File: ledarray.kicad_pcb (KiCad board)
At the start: 2 copper layers, 37.6 x 52.3 mm, 37 parts, among them J1 Conn_01x14_Male, J2 Conn_01x14_Male

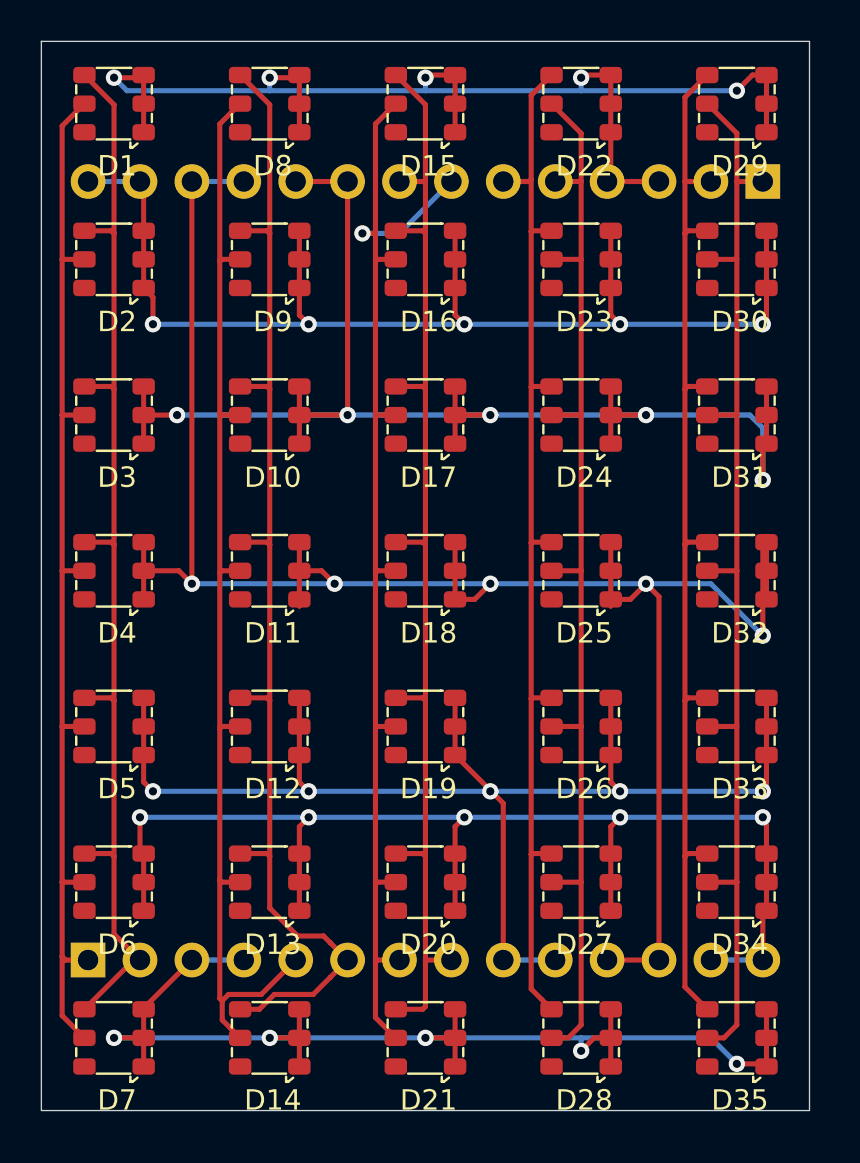
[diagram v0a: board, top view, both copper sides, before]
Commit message: Add reversed LED polarity variant
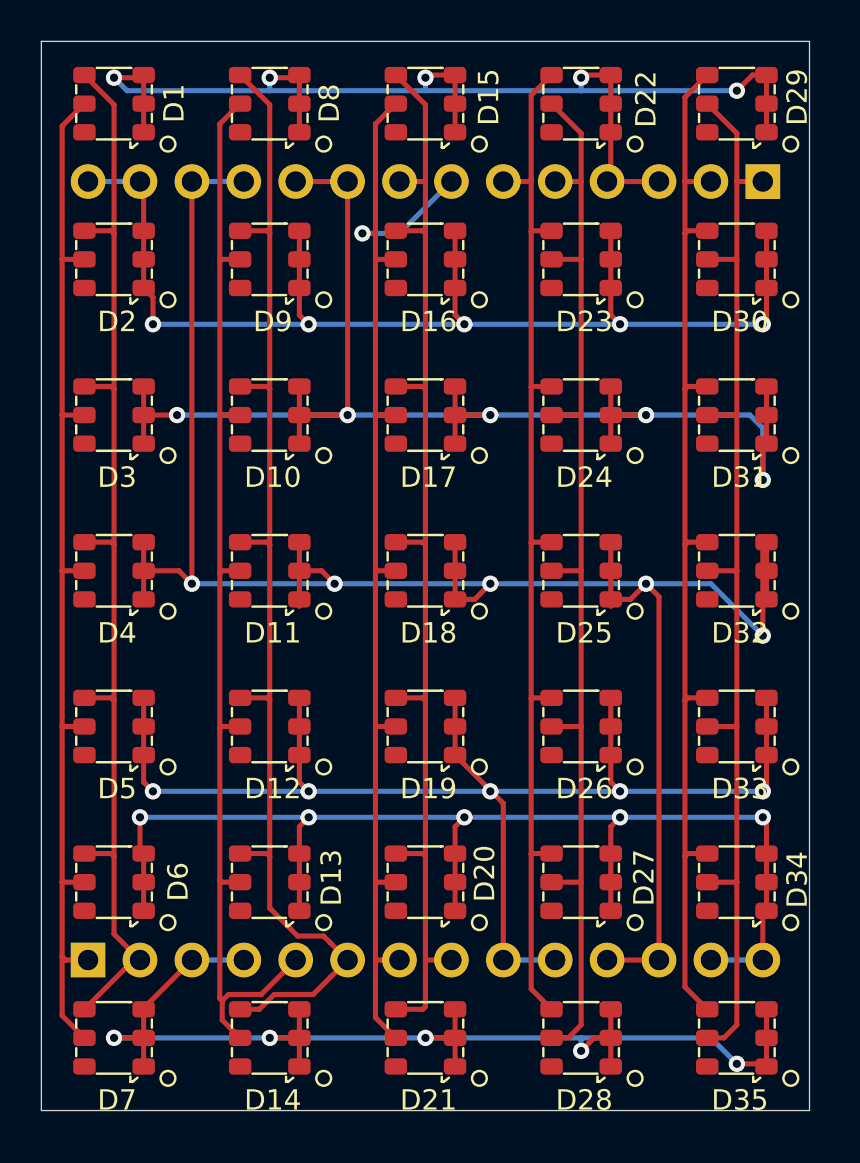
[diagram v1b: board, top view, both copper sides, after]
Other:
- board text added: "Design by Kliment github.com/kliment/5x7RGmatrix COMMON CATHODE VERSION"
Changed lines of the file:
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@@
   (general
     (thickness 1.6)
-    (drawings 4)
+    (drawings 40)
     (tracks 387)
     (zones 0)
@@
     (descr "Through hole straight pin header, 1x14, 2.54mm pitch, single row")
     (tags "Through hole pin header THT 1x14 2.54mm single row")
-    (fp_text reference J2 (at 0 2.33 90) (layer B.SilkS)
+    (fp_text reference J2 (at -2.67 -17.21 180) (layer B.SilkS)
       (effects (font (size 1 1) (thickness 0.15)) (justify mirror))
     )
@@
     (descr "Through hole straight pin header, 1x14, 2.54mm pitch, single row")
     (tags "Through hole pin header THT 1x14 2.54mm single row")
-    (fp_text reference J1 (at 0 2.33 90) (layer B.SilkS)
+    (fp_text reference J1 (at -2.53 -17.01 180) (layer B.SilkS)
       (effects (font (size 1 1) (thickness 0.15)) (justify mirror))
     )
@@
   (module corelib:FM-Z3535RGBA-SH (layer F.Cu)
     (at 180.34 109.22)
-    (fp_text reference D34 (at 0.15 3.05) (layer F.SilkS)
+    (fp_text reference D34 (at 2.96 -0.12 90) (layer F.SilkS)
       (effects (font (size 1 1) (thickness 0.15)))
     )
@@
   (module corelib:FM-Z3535RGBA-SH (layer F.Cu)
     (at 180.34 71.12)
-    (fp_text reference D29 (at 0.15 3.05) (layer F.SilkS)
+    (fp_text reference D29 (at 2.96 -0.32 90) (layer F.SilkS)
       (effects (font (size 1 1) (thickness 0.15)))
     )
@@
   (module corelib:FM-Z3535RGBA-SH (layer F.Cu)
     (at 172.72 109.22)
-    (fp_text reference D27 (at 0.15 3.05) (layer F.SilkS)
+    (fp_text reference D27 (at 3.08 -0.22 90) (layer F.SilkS)
       (effects (font (size 1 1) (thickness 0.15)))
     )
@@
   (module corelib:FM-Z3535RGBA-SH (layer F.Cu)
     (at 172.72 71.12)
-    (fp_text reference D22 (at 0.15 3.05) (layer F.SilkS)
+    (fp_text reference D22 (at 3.18 -0.22 90) (layer F.SilkS)
       (effects (font (size 1 1) (thickness 0.15)))
     )
@@
   (module corelib:FM-Z3535RGBA-SH (layer F.Cu)
     (at 165.1 109.22)
-    (fp_text reference D20 (at 0.15 3.05) (layer F.SilkS)
+    (fp_text reference D20 (at 2.9 -0.42 90) (layer F.SilkS)
       (effects (font (size 1 1) (thickness 0.15)))
     )
@@
   (module corelib:FM-Z3535RGBA-SH (layer F.Cu)
     (at 165.1 71.12)
-    (fp_text reference D15 (at 0.15 3.05) (layer F.SilkS)
+    (fp_text reference D15 (at 3.1 -0.32 90) (layer F.SilkS)
       (effects (font (size 1 1) (thickness 0.15)))
     )
@@
   (module corelib:FM-Z3535RGBA-SH (layer F.Cu)
     (at 157.48 109.22)
-    (fp_text reference D13 (at 0.15 3.05) (layer F.SilkS)
+    (fp_text reference D13 (at 3.02 -0.22 90) (layer F.SilkS)
       (effects (font (size 1 1) (thickness 0.15)))
     )
@@
   (module corelib:FM-Z3535RGBA-SH (layer F.Cu)
     (at 157.48 71.12)
-    (fp_text reference D8 (at 0.15 3.05) (layer F.SilkS)
+    (fp_text reference D8 (at 2.92 -0.02 90) (layer F.SilkS)
       (effects (font (size 1 1) (thickness 0.15)))
     )
@@
   (module corelib:FM-Z3535RGBA-SH (layer F.Cu)
     (at 149.86 109.22)
-    (fp_text reference D6 (at 0.15 3.05) (layer F.SilkS)
+    (fp_text reference D6 (at 3.14 -0.02 90) (layer F.SilkS)
       (effects (font (size 1 1) (thickness 0.15)))
     )
@@
   (module corelib:FM-Z3535RGBA-SH (layer F.Cu)
     (at 149.86 71.12)
-    (fp_text reference D1 (at 0.15 3.05) (layer F.SilkS)
+    (fp_text reference D1 (at 2.94 -0.02 90) (layer F.SilkS)
       (effects (font (size 1 1) (thickness 0.15)))
     )
@@
       (net 4 /17))
   )
+  (gr_text "Design by Kliment\ngithub.com/kliment/5x7RGmatrix\nCOMMON CATHODE VERSION" (at 164.5 93.1) (layer B.SilkS)
+    (effects (font (size 1 1) (thickness 0.15)) (justify mirror))
+  )
+  (gr_circle (center 182.98 118.82) (end 183.18 119.12) (layer F.SilkS) (width 0.12))
+  (gr_circle (center 175.36 118.82) (end 175.56 119.12) (layer F.SilkS) (width 0.12))
+  (gr_circle (center 167.74 118.82) (end 167.94 119.12) (layer F.SilkS) (width 0.12))
+  (gr_circle (center 160.12 118.82) (end 160.32 119.12) (layer F.SilkS) (width 0.12))
+  (gr_circle (center 152.5 118.82) (end 152.7 119.12) (layer F.SilkS) (width 0.12))
+  (gr_circle (center 182.98 111.2) (end 183.18 111.5) (layer F.SilkS) (width 0.12))
+  (gr_circle (center 175.36 111.2) (end 175.56 111.5) (layer F.SilkS) (width 0.12))
+  (gr_circle (center 167.74 111.2) (end 167.94 111.5) (layer F.SilkS) (width 0.12))
+  (gr_circle (center 160.12 111.2) (end 160.32 111.5) (layer F.SilkS) (width 0.12))
+  (gr_circle (center 152.5 111.2) (end 152.7 111.5) (layer F.SilkS) (width 0.12))
+  (gr_circle (center 182.98 103.58) (end 183.18 103.88) (layer F.SilkS) (width 0.12))
+  (gr_circle (center 175.36 103.58) (end 175.56 103.88) (layer F.SilkS) (width 0.12))
+  (gr_circle (center 167.74 103.58) (end 167.94 103.88) (layer F.SilkS) (width 0.12))
+  (gr_circle (center 160.12 103.58) (end 160.32 103.88) (layer F.SilkS) (width 0.12))
+  (gr_circle (center 152.5 103.58) (end 152.7 103.88) (layer F.SilkS) (width 0.12))
+  (gr_circle (center 182.98 95.96) (end 183.18 96.26) (layer F.SilkS) (width 0.12))
+  (gr_circle (center 175.36 95.96) (end 175.56 96.26) (layer F.SilkS) (width 0.12))
+  (gr_circle (center 167.74 95.96) (end 167.94 96.26) (layer F.SilkS) (width 0.12))
+  (gr_circle (center 160.12 95.96) (end 160.32 96.26) (layer F.SilkS) (width 0.12))
+  (gr_circle (center 152.5 95.96) (end 152.7 96.26) (layer F.SilkS) (width 0.12))
+  (gr_circle (center 182.98 88.34) (end 183.18 88.64) (layer F.SilkS) (width 0.12))
+  (gr_circle (center 175.36 88.34) (end 175.56 88.64) (layer F.SilkS) (width 0.12))
+  (gr_circle (center 167.74 88.34) (end 167.94 88.64) (layer F.SilkS) (width 0.12))
+  (gr_circle (center 160.12 88.34) (end 160.32 88.64) (layer F.SilkS) (width 0.12))
+  (gr_circle (center 152.5 88.34) (end 152.7 88.64) (layer F.SilkS) (width 0.12))
+  (gr_circle (center 182.98 80.72) (end 183.18 81.02) (layer F.SilkS) (width 0.12))
+  (gr_circle (center 175.36 80.72) (end 175.56 81.02) (layer F.SilkS) (width 0.12))
+  (gr_circle (center 167.74 80.72) (end 167.94 81.02) (layer F.SilkS) (width 0.12))
+  (gr_circle (center 160.12 80.72) (end 160.32 81.02) (layer F.SilkS) (width 0.12))
+  (gr_circle (center 152.5 80.72) (end 152.7 81.02) (layer F.SilkS) (width 0.12))
+  (gr_circle (center 182.98 73.1) (end 183.18 73.4) (layer F.SilkS) (width 0.12))
+  (gr_circle (center 175.36 73.1) (end 175.56 73.4) (layer F.SilkS) (width 0.12))
+  (gr_circle (center 167.74 73.1) (end 167.94 73.4) (layer F.SilkS) (width 0.12))
+  (gr_circle (center 160.12 73.1) (end 160.32 73.4) (layer F.SilkS) (width 0.12))
+  (gr_circle (center 152.5 73.1) (end 152.7 73.4) (layer F.SilkS) (width 0.12))
   (gr_line (start 183.896 68.072) (end 183.896 120.396) (layer Edge.Cuts) (width 0.05))
   (gr_line (start 146.304 68.072) (end 183.896 68.072) (layer Edge.Cuts) (width 0.05))

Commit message: Delete cache file from repo, update silkscreen on CC variant
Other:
- board text added: "Design by Kliment github.com/kliment/5x7RGmatrix ROW CATHODE COLUMN ANODE VERSION"
- board text removed: "Design by Kliment github.com/kliment/5x7RGmatrix COMMON CATHODE VERSION"
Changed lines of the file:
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@@
       (net 4 /17))
   )
-  (gr_text "Design by Kliment\ngithub.com/kliment/5x7RGmatrix\nCOMMON CATHODE VERSION" (at 164.5 93.1) (layer B.SilkS)
+  (gr_text "Design by Kliment\ngithub.com/kliment/5x7RGmatrix\nROW CATHODE COLUMN ANODE VERSION" (at 164.5 93.1) (layer B.SilkS)
     (effects (font (size 1 1) (thickness 0.15)) (justify mirror))
   )
